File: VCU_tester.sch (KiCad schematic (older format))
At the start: 50 parts, among them J1 Conn_01x04_Male, J2 Screw_Terminal_01x02, J500 Conn_01x08_Female, J501 Conn_01x08_Female, J502 Conn_01x08_Female, J504 Conn_02x18_Odd_Even, J505 Conn_01x08_Female, J506 Conn_01x08_Female, J507 Conn_01x08_Female, P8 BeagleBone_Black_Header, P9 BeagleBone_Black_Header

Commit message: removed dac, added jumpers, ready for parting up
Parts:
- removed C?: 100p, symbol Device:C
- removed C?: 10u, symbol Device:C
- removed TP11, TP12, TP13, TP14, TP15, TP9, TP? (x5): TestPoint, symbol Connector:TestPoint
- removed U?: TLV5631IDW, DW0020A_N, symbol TLV5631IDW:TLV5631IDW
- added D2: LED, symbol Device:LED
- added J7: Conn_01x04_Male, symbol Connector:Conn_01x04_Male
- added R3: 150R, symbol Device:R_Small
- added R4, R5, R6: 100R, symbol Device:R_Small
- D1: value LED_ABRG -> LED_RABG; symbol Device:LED_ABRG -> Device:LED_RABG; Part (none) -> WP154A4SEJ3VBDZGW/CA
- gave numbers to parts that had none: 16
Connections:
- net labels added: VCUGPIO_12
- net labels removed: BBLR, BBLT, BBRT, GPIO_14, GPIO_15, GPIO_20, VCULR, VCULT, VCURR, VCURT
- wire segments 256 -> 238
- no-connect marks 88 -> 106
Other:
- note added: "BBUART1 -> UART3 on VCU"
- note added: "CurrSense (!!!!)\nDO WE HAVE THIS CONN?"
- note added: "External power/reset\n(if we get a case)"
- note removed: "BBUART4 -> UART on VCU (not UART1)"
- note removed: "CHECK!!\nCSO may not be appropriate.\nTiming may need to be modified.\n\nDatasheet is a mess.\nNo SPI support but it says it does??"
- note removed: "CurrSense (!!!!)\nWhere is this conn????"
- note removed: "VCU SPI DAC 8ch"
- moved on the sheet: J1, J2, TP17, TP18, TP19, TP20, TP21, TP40, TP41, TP42, TP43, TP44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

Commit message: parts assigned, layout started, CAN and RS232 sides done
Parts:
- removed P1: USB_C_Plug_USB2.0, symbol Connector:USB_C_Plug_USB2.0
- removed TP17, TP18, TP19, TP20, TP21, TP40, TP41, TP42, TP5, TP6, TP7, TP8: TestPoint, symbol Connector:TestPoint
- added J12, J13: Conn_01x08_Male, Connector_PinHeader_2.54mm:PinHeader_1x08_P2.54mm_Vertical, symbol Connector:Conn_01x08_Male
- D1: footprint (none) -> LED_THT:LED_D5.0mm-4_RGB
- D2: footprint (none) -> Diode_SMD:D_1210_3225Metric_Pad1.42x2.65mm_HandSolder
- J1, J7: footprint (none) -> Connector_PinHeader_2.54mm:PinHeader_1x04_P2.54mm_Vertical
- J2: footprint (none) -> TerminalBlock:TerminalBlock_bornier-2_P5.08mm; Part (none) -> 282837-2
- J500, J501, J502, J506, J507: footprint (none) -> Connector_PinSocket_2.54mm:PinSocket_1x08_P2.54mm_Vertical
- J504: footprint (none) -> Connector_PinSocket_2.54mm:PinSocket_2x18_P2.54mm_Vertical
- J505: value Conn_01x08_Female -> Conn_01x10_Female; footprint (none) -> Connector_PinSocket_2.54mm:PinSocket_1x10_P2.54mm_Vertical
- P8, P9: Part (none) -> 1528-1365-ND
- R3: value 150R -> 47R; footprint (none) -> Resistor_SMD:R_0805_2012Metric_Pad1.15x1.40mm_HandSolder
- R4, R5: value 100R -> 20R; footprint (none) -> Resistor_SMD:R_0805_2012Metric_Pad1.15x1.40mm_HandSolder
- R6: footprint (none) -> Resistor_SMD:R_0805_2012Metric_Pad1.15x1.40mm_HandSolder
- TP1, TP2, TP3, TP4, TP43, TP44, TP45, TP46, TP47, TP48: footprint (none) -> Connector_PinHeader_2.54mm:PinHeader_1x01_P2.54mm_Vertical
- U1: Part (none) -> 296-26321-1-ND
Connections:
- wire segments 238 -> 240
- no-connect marks 106 -> 93
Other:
- note added: "Analog inputs (Future use)"
- note added: "Draw = 500mA approx ?"
- note added: "Draw approx 500mA"
- note added: "POWER FROM EXTERNAL BARREL JACK\nUSB NOT SUFFICIENT"
- note removed: "Power / Serial iface (todo?)"
- moved on the sheet: TP43, TP44, TP45, TP46, TP47, TP48

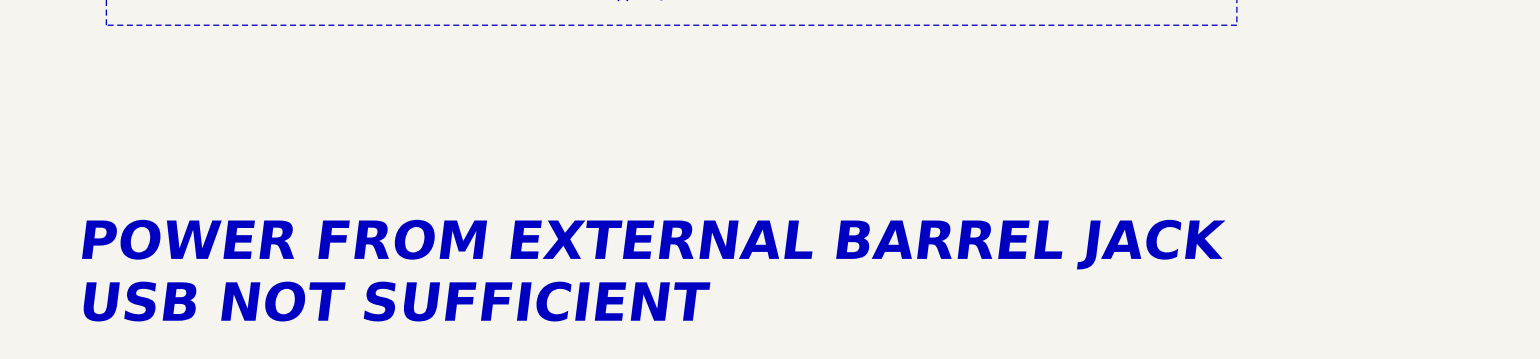
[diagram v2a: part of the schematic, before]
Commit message: added worksheet, shuffled board around to make it smaller
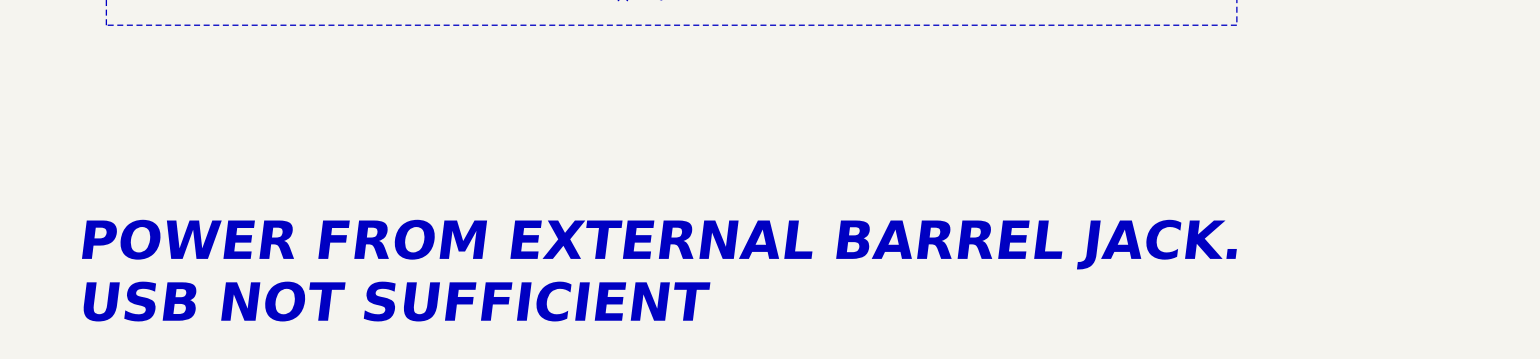
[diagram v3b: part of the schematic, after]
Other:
- note added: "POWER FROM EXTERNAL BARREL JACK.\nUSB NOT SUFFICIENT"
- note removed: "POWER FROM EXTERNAL BARREL JACK\nUSB NOT SUFFICIENT"
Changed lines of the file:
@@
 encoding utf-8
 Sheet 1 3
-Title ""
-Date ""
-Rev ""
+Title "VCU Test Board"
+Date "2020-02-16"
+Rev "-"
 Comp ""
 Comment1 ""
@@
 $EndComp
 Text Notes 800  11000 0    197  Italic 39
-POWER FROM EXTERNAL BARREL JACK\nUSB NOT SUFFICIENT
+POWER FROM EXTERNAL BARREL JACK.\nUSB NOT SUFFICIENT
 Wire Wire Line
 	13700 7000 14200 7000

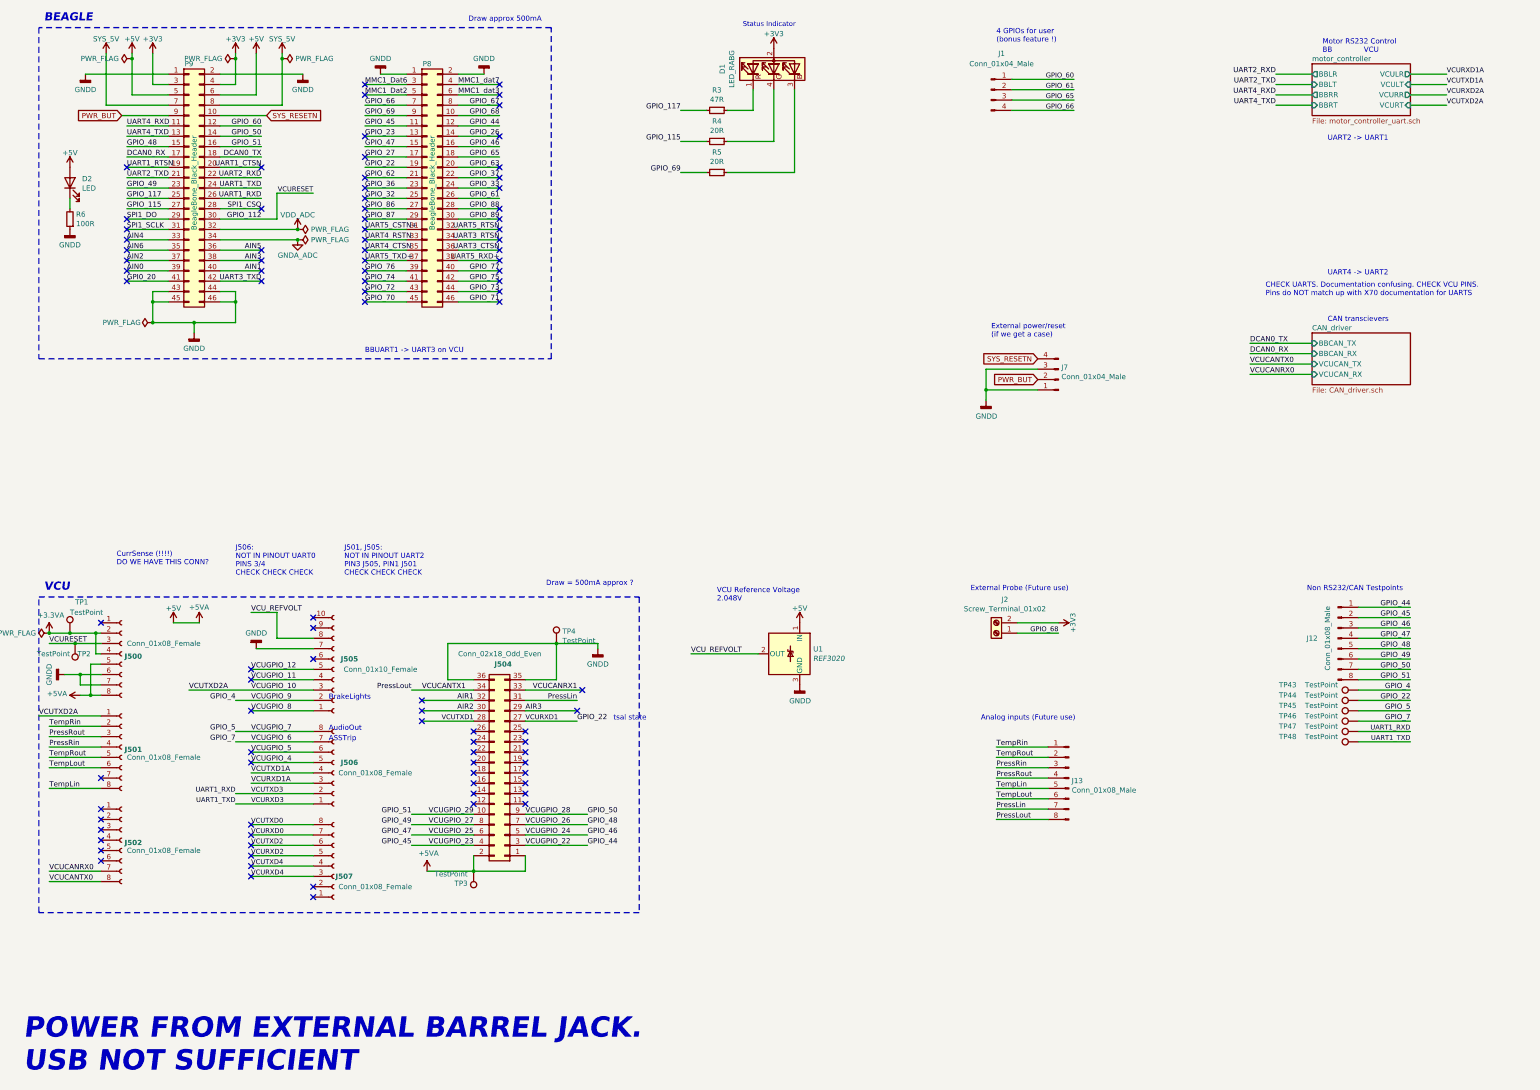
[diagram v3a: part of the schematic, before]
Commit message: pins corrected, RTC added
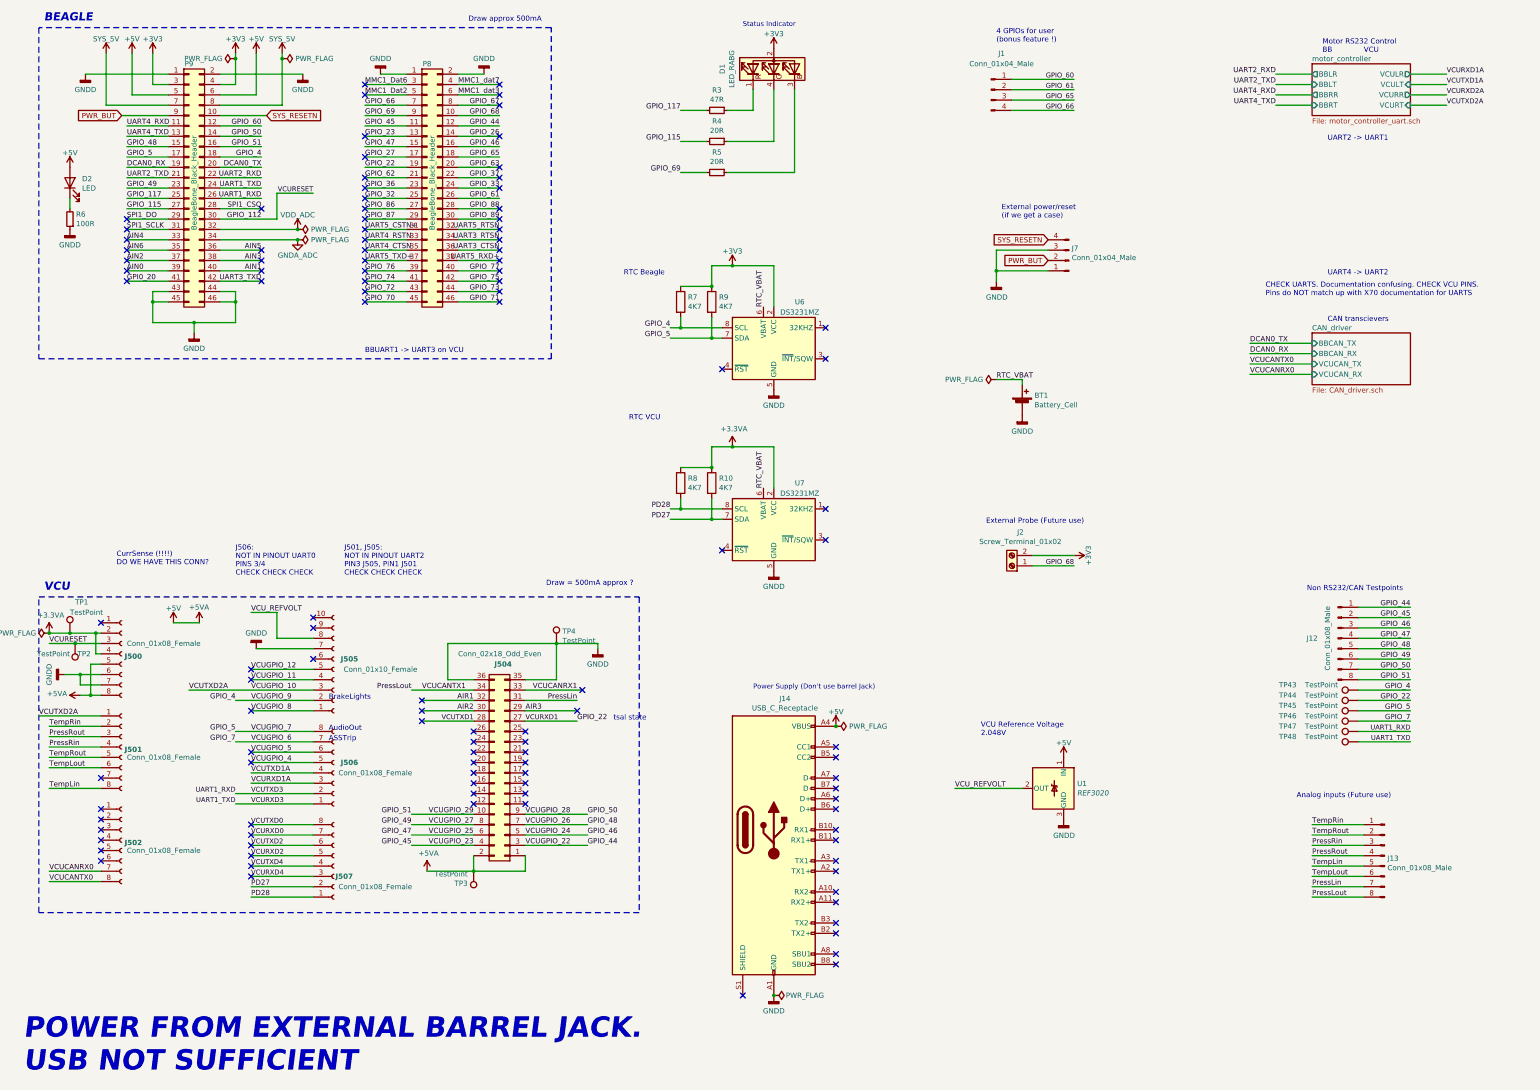
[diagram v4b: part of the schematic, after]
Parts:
- added BT1: Battery_Cell, Battery:BatteryHolder_MPD_BC2003_1x2032, symbol Device:Battery_Cell
- added J14: USB_C_Receptacle, Connector_USB:USB_C_Receptacle_GCT_USB4085, symbol Connector:USB_C_Receptacle
- added R10, R7, R8, R9: 4K7, Resistor_SMD:R_0805_2012Metric_Pad1.15x1.40mm_HandSolder, symbol Device:R
- added U6, U7: DS3231MZ, Package_SO:SOIC-8_3.9x4.9mm_P1.27mm, symbol Timer_RTC:DS3231MZ
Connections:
- net UART1_CTSN is gone; now on net DCAN0_TX: P9.20 (Pin_20)
- net UART1_RTSN is gone; now on net DCAN0_RX: P9.19 (Pin_19)
- net +3.3VA: now also R10.1, R8.1, U7.2 (VCC)
- net +3V3: now also R7.1, R9.1, U6.2 (VCC)
- net +5V: now also J14.A4 (VBUS), J14.A9 (VBUS), J14.B4 (VBUS), J14.B9 (VBUS)
- net DCAN0_RX: no longer P9.17 (Pin_17)
- net DCAN0_TX: no longer P9.18 (Pin_18)
- net GNDD: now also BT1.2 (-), J14.A1 (GND), J14.A12 (GND), J14.B1 (GND), J14.B12 (GND), U6.5 (GND), U7.5 (GND)
- net GPIO_4: now also P9.18 (Pin_18), R7.2, U6.8 (SCL)
- net GPIO_5: now also P9.17 (Pin_17), R9.2, U6.7 (SDA)
- net PD28: now reaches J507.1 (Pin_1)
- net PD28: now also R8.2, U7.8 (SCL)
- net PD27: now reaches J507.2 (Pin_2)
- net PD27: now also R10.2, U7.7 (SDA)
- new net RTC_VBAT: BT1.1 (+), U6.6 (VBAT), U7.6 (VBAT)
- no-connect marks 93 -> 112
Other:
- note added: "Power Supply (Don't use barrel Jack)"
- note added: "RTC Beagle"
- note added: "RTC VCU"
- moved on the sheet: J13, J2, J7, U1

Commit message: routing start
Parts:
- added J15: USB_B_Micro, symbol Connector:USB_B_Micro
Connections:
- net +5V: now also J15.1 (VBUS)
- net GNDD: now also J15.5 (GND)
- no-connect marks 112 -> 116
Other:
- note removed: "POWER FROM EXTERNAL BARREL JACK.\nUSB NOT SUFFICIENT"
- moved on the sheet: J14, U1
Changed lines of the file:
@@
 	1    0    0    -1
 $EndComp
-Text Notes 800  11000 0    197  Italic 39
-POWER FROM EXTERNAL BARREL JACK.\nUSB NOT SUFFICIENT
 Wire Wire Line
 	13700 7000 14200 7000
@@
 L power:PWR_FLAG #FLG0104
 U 1 1 5F1D987B
-P 8050 10250
-F 0 "#FLG0104" H 8050 10325 50  0001 C CNN
-F 1 "PWR_FLAG" V 8050 10550 50  0000 C CNN
-F 2 "" H 8050 10250 50  0001 C CNN
-F 3 "~" H 8050 10250 50  0001 C CNN
-	1    8050 10250
+P 7550 9950
+F 0 "#FLG0104" H 7550 10025 50  0001 C CNN
+F 1 "PWR_FLAG" V 7550 10250 50  0000 C CNN
+F 2 "" H 7550 9950 50  0001 C CNN
+F 3 "~" H 7550 9950 50  0001 C CNN
+	1    7550 9950
 	0    1    1    0
 $EndComp
@@
 L power:PWR_FLAG #FLG0105
 U 1 1 5F25691E
-P 8650 7650
-F 0 "#FLG0105" H 8650 7725 50  0001 C CNN
-F 1 "PWR_FLAG" V 8650 7777 50  0000 L CNN
-F 2 "" H 8650 7650 50  0001 C CNN
-F 3 "~" H 8650 7650 50  0001 C CNN
-	1    8650 7650
+P 8150 7350
+F 0 "#FLG0105" H 8150 7425 50  0001 C CNN
+F 1 "PWR_FLAG" V 8150 7477 50  0000 L CNN
+F 2 "" H 8150 7350 50  0001 C CNN
+F 3 "~" H 8150 7350 50  0001 C CNN
+	1    8150 7350
 	0    1    1    0
 $EndComp
@@
 L Connector:USB_C_Receptacle J14
 U 1 1 5FE022B2
-P 8050 8650
-F 0 "J14" H 8157 9917 50  0000 C CNN
-F 1 "USB_C_Receptacle" H 8157 9826 50  0000 C CNN
-F 2 "Connector_USB:USB_C_Receptacle_GCT_USB4085" H 8200 8650 50  0001 C CNN
-F 3 "https://www.usb.org/sites/default/files/documents/usb_type-c.zip" H 8200 8650 50  0001 C CNN
-F 4 "2073-USB4085-GF-ACT-ND" H 8050 8650 50  0001 C CNN "Part"
-	1    8050 8650
-	1    0    0    -1
-$EndComp
-NoConn ~ 7750 10250
-NoConn ~ 8650 8450
-NoConn ~ 8650 8350
-NoConn ~ 8650 8250
-NoConn ~ 8650 8150
-NoConn ~ 8650 9650
-NoConn ~ 8650 9550
-NoConn ~ 8650 9350
-NoConn ~ 8650 9250
-NoConn ~ 8650 9050
-NoConn ~ 8650 8950
-NoConn ~ 8650 8650
-NoConn ~ 8650 8750
-NoConn ~ 8650 9950
-NoConn ~ 8650 9850
-NoConn ~ 8650 7950
-NoConn ~ 8650 7850
+P 7550 8350
+F 0 "J14" H 7657 9617 50  0000 C CNN
+F 1 "USB_C_Receptacle" H 7657 9526 50  0000 C CNN
+F 2 "Connector_USB:USB_C_Receptacle_GCT_USB4085" H 7700 8350 50  0001 C CNN
+F 3 "https://www.usb.org/sites/default/files/documents/usb_type-c.zip" H 7700 8350 50  0001 C CNN
+F 4 "2073-USB4085-GF-ACT-ND" H 7550 8350 50  0001 C CNN "Part"
+	1    7550 8350
+	1    0    0    -1
+$EndComp
+NoConn ~ 7250 9950
+NoConn ~ 8150 8150
+NoConn ~ 8150 8050
+NoConn ~ 8150 7950
+NoConn ~ 8150 7850
+NoConn ~ 8150 9350
+NoConn ~ 8150 9250
+NoConn ~ 8150 9050
+NoConn ~ 8150 8950
+NoConn ~ 8150 8750
+NoConn ~ 8150 8650
+NoConn ~ 8150 8350
+NoConn ~ 8150 8450
+NoConn ~ 8150 9650
+NoConn ~ 8150 9550
+NoConn ~ 8150 7650
+NoConn ~ 8150 7550
 $Comp
 L power:GNDD #PWR0103
 U 1 1 5FFC2327
-P 8050 10250
-F 0 "#PWR0103" H 8050 10000 50  0001 C CNN
-F 1 "GNDD" H 8050 10100 50  0000 C CNN
-F 2 "" H 8050 10250 60  0000 C CNN
-F 3 "" H 8050 10250 60  0000 C CNN
-	1    8050 10250
-	1    0    0    -1
-$EndComp
-Connection ~ 8050 10250
+P 7550 9950
+F 0 "#PWR0103" H 7550 9700 50  0001 C CNN
+F 1 "GNDD" H 7550 9800 50  0000 C CNN
+F 2 "" H 7550 9950 60  0000 C CNN
+F 3 "" H 7550 9950 60  0000 C CNN
+	1    7550 9950
+	1    0    0    -1
+$EndComp
+Connection ~ 7550 9950
 $Comp
 L power:+5V #PWR0116
 U 1 1 5FFD476B
-P 8650 7650
-F 0 "#PWR0116" H 8650 7500 50  0001 C CNN
-F 1 "+5V" H 8650 7790 50  0000 C CNN
-F 2 "" H 8650 7650 60  0000 C CNN
-F 3 "" H 8650 7650 60  0000 C CNN
-	1    8650 7650
-	1    0    0    -1
-$EndComp
-Text Notes 7850 7300 0    47   ~ 0
+P 8150 7350
+F 0 "#PWR0116" H 8150 7200 50  0001 C CNN
+F 1 "+5V" H 8150 7490 50  0000 C CNN
+F 2 "" H 8150 7350 60  0000 C CNN
+F 3 "" H 8150 7350 60  0000 C CNN
+	1    8150 7350
+	1    0    0    -1
+$EndComp
+Text Notes 7350 7000 0    47   ~ 0
 Power Supply (Don't use barrel Jack)
-Connection ~ 8650 7650
+Connection ~ 8150 7350
 Wire Wire Line
 	2200 2150 1800 2150
@@
 RTC VCU
 Wire Wire Line
-	9800 8250 10450 8250
-Text Label 9800 8250 0    50   ~ 0
+	10750 8450 11400 8450
+Text Label 10750 8450 0    50   ~ 0
 VCU_REFVOLT
 $Comp
 L Reference_Voltage:REF3020 U1
 U 1 1 5F9A6E14
-P 10750 8250
-F 0 "U1" H 10520 8296 50  0000 R CNN
-F 1 "REF3020" H 10520 8205 50  0000 R CIN
-F 2 "Package_TO_SOT_SMD:SOT-23" H 10750 7800 50  0001 C CIN
-F 3 "http://www.ti.com/lit/ds/symlink/ref3033.pdf" H 10850 7900 50  0001 C CIN
-F 4 "296-26321-1-ND" H 10750 8250 50  0001 C CNN "Part"
-	1    10750 8250
+P 11700 8450
+F 0 "U1" H 11470 8496 50  0000 R CNN
+F 1 "REF3020" H 11470 8405 50  0000 R CIN
+F 2 "Package_TO_SOT_SMD:SOT-23" H 11700 8000 50  0001 C CIN
+F 3 "http://www.ti.com/lit/ds/symlink/ref3033.pdf" H 11800 8100 50  0001 C CIN
+F 4 "296-26321-1-ND" H 11700 8450 50  0001 C CNN "Part"
+	1    11700 8450
 	-1   0    0    -1
 $EndComp
@@
 L power:GNDD #PWR0104
 U 1 1 5F9A8026
-P 10850 8550
-F 0 "#PWR0104" H 10850 8300 50  0001 C CNN
-F 1 "GNDD" H 10854 8395 50  0000 C CNN
-F 2 "" H 10850 8550 50  0001 C CNN
-F 3 "" H 10850 8550 50  0001 C CNN
-	1    10850 8550
+P 11800 8750
+F 0 "#PWR0104" H 11800 8500 50  0001 C CNN
+F 1 "GNDD" H 11804 8595 50  0000 C CNN
+F 2 "" H 11800 8750 50  0001 C CNN
+F 3 "" H 11800 8750 50  0001 C CNN
+	1    11800 8750
 	1    0    0    -1
 $EndComp
@@
 L power:+5V #PWR0105
 U 1 1 5F9AA125
-P 10850 7950
-F 0 "#PWR0105" H 10850 7800 50  0001 C CNN
-F 1 "+5V" H 10850 8090 50  0000 C CNN
-F 2 "" H 10850 7950 60  0000 C CNN
-F 3 "" H 10850 7950 60  0000 C CNN
-	1    10850 7950
-	1    0    0    -1
-$EndComp
-Text Notes 10050 7750 0    50   ~ 0
+P 11800 8150
+F 0 "#PWR0105" H 11800 8000 50  0001 C CNN
+F 1 "+5V" H 11800 8290 50  0000 C CNN
+F 2 "" H 11800 8150 60  0000 C CNN
+F 3 "" H 11800 8150 60  0000 C CNN
+	1    11800 8150
+	1    0    0    -1
+$EndComp
+Text Notes 11000 7950 0    50   ~ 0
 VCU Reference Voltage\n2.048V
 $Comp
@@
 	0    -1   -1   0
 $EndComp
+$Comp
+L Connector:USB_B_Micro J15
+U 1 1 60933E7E
+P 8800 8200
+F 0 "J15" H 8857 8667 50  0000 C CNN
+F 1 "USB_B_Micro" H 8857 8576 50  0000 C CNN
+F 2 "" H 8950 8150 50  0001 C CNN
+F 3 "~" H 8950 8150 50  0001 C CNN
+	1    8800 8200
+	1    0    0    -1
+$EndComp
+NoConn ~ 8700 8600
+NoConn ~ 9100 8300
+NoConn ~ 9100 8200
+NoConn ~ 9100 8400
+$Comp
+L power:GNDD #PWR019
+U 1 1 6099CF5B
+P 8800 8600
+F 0 "#PWR019" H 8800 8350 50  0001 C CNN
+F 1 "GNDD" H 8800 8450 50  0000 C CNN
+F 2 "" H 8800 8600 60  0000 C CNN
+F 3 "" H 8800 8600 60  0000 C CNN
+	1    8800 8600
+	1    0    0    -1
+$EndComp
+$Comp
+L power:+5V #PWR020
+U 1 1 6099D494
+P 9100 8000
+F 0 "#PWR020" H 9100 7850 50  0001 C CNN
+F 1 "+5V" H 9100 8140 50  0000 C CNN
+F 2 "" H 9100 8000 60  0000 C CNN
+F 3 "" H 9100 8000 60  0000 C CNN
+	1    9100 8000
+	0    1    1    0
+$EndComp
 $EndSCHEMATC

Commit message: cant remember what I added Im tired
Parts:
- J15: footprint (none) -> Connector_USB:USB_Micro-B_Molex-105017-0001
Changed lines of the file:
@@
 F 0 "J15" H 8857 8667 50  0000 C CNN
 F 1 "USB_B_Micro" H 8857 8576 50  0000 C CNN
-F 2 "" H 8950 8150 50  0001 C CNN
+F 2 "Connector_USB:USB_Micro-B_Molex-105017-0001" H 8950 8150 50  0001 C CNN
 F 3 "~" H 8950 8150 50  0001 C CNN
 	1    8800 8200
